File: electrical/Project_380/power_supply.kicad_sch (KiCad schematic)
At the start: 7 parts, among them J5 FL_Motor, J6 FL_Motor, J7 FL_Motor, J8 FL_Motor, U1 HW613

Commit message: added downforce motor control pin
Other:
- title: (none) -> Power Supply
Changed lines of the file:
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@@
 (kicad_sch (version 20211123) (generator eeschema)
   (paper "A4")
+  (title_block
+    (title "Power Supply")
+    (date "2022-02-03")
+    (rev "1.0")
+  )
   (junction (at 48.006 93.726) (diameter 0) (color 0 0 0 0)
   )

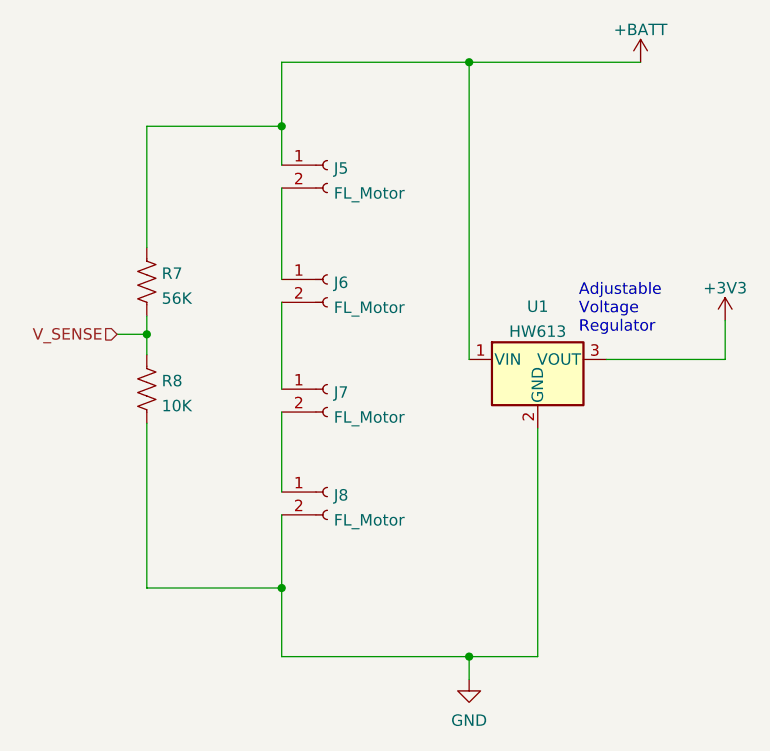
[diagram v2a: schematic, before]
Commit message: added motor controller
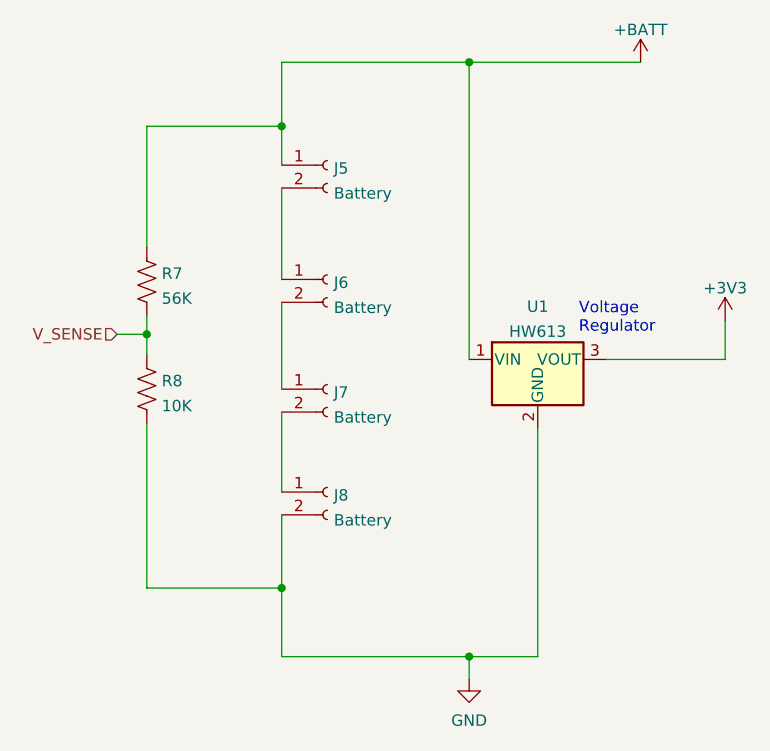
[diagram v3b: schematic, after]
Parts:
- J5, J6, J7, J8: value FL_Motor -> Battery; footprint (none) -> Connector_PinHeader_1.00mm:PinHeader_1x02_P1.00mm_Vertical
- R7, R8: footprint (none) -> Resistor_SMD:R_0603_1608Metric
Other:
- note added: "Voltage Regulator"
- note removed: "Adjustable Voltage Regulator"
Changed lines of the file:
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@@
     (stroke (width 0) (type default) (color 0 0 0 0))
   )
-  (text "Adjustable\nVoltage\nRegulator\n" (at 96.012 93.726 0)
+  (text "Voltage\nRegulator\n" (at 96.012 93.726 0)
     (effects (font (size 1.27 1.27)) (justify left bottom))
   )
@@
   (symbol (lib_id "power:GND") (at 83.82 132.08 0) (unit 1)
     (in_bom yes) (on_board yes) (fields_autoplaced)
-    (property "Reference" "#PWR?" (id 0) (at 83.82 138.43 0)
+    (property "Reference" "#PWR0112" (id 0) (at 83.82 138.43 0)
       (effects (font (size 1.27 1.27)) hide)
     )
@@
       (effects (font (size 1.27 1.27)) (justify right))
     )
-    (property "Footprint" "" (id 2) (at 46.99 87.63 90)
+    (property "Footprint" "Resistor_SMD:R_0603_1608Metric" (id 2) (at 46.99 87.63 90)
       (effects (font (size 1.27 1.27)) hide)
     )
@@
       (effects (font (size 1.27 1.27)) (justify right))
     )
-    (property "Footprint" "" (id 2) (at 46.99 99.568 90)
+    (property "Footprint" "Resistor_SMD:R_0603_1608Metric" (id 2) (at 46.99 99.568 90)
       (effects (font (size 1.27 1.27)) hide)
     )
@@
       (effects (font (size 1.27 1.27)) (justify left))
     )
-    (property "Value" "FL_Motor" (id 1) (at 68.7832 102.9586 0)
+    (property "Value" "Battery" (id 1) (at 68.7832 102.9586 0)
       (effects (font (size 1.27 1.27)) (justify left))
     )
-    (property "Footprint" "" (id 2) (at 68.072 99.822 0)
+    (property "Footprint" "Connector_PinHeader_1.00mm:PinHeader_1x02_P1.00mm_Vertical" (id 2) (at 68.072 99.822 0)
       (effects (font (size 1.27 1.27)) hide)
     )
@@
   (symbol (lib_id "power:+3V3") (at 112.268 92.202 0) (unit 1)
     (in_bom yes) (on_board yes) (fields_autoplaced)
-    (property "Reference" "#PWR?" (id 0) (at 112.268 96.012 0)
+    (property "Reference" "#PWR0114" (id 0) (at 112.268 96.012 0)
       (effects (font (size 1.27 1.27)) hide)
     )
@@
   (symbol (lib_id "power:+BATT") (at 102.87 63.5 0) (unit 1)
     (in_bom yes) (on_board yes) (fields_autoplaced)
-    (property "Reference" "#PWR?" (id 0) (at 102.87 67.31 0)
+    (property "Reference" "#PWR0113" (id 0) (at 102.87 67.31 0)
       (effects (font (size 1.27 1.27)) hide)
     )
@@
       (effects (font (size 1.27 1.27)) (justify left))
     )
-    (property "Value" "FL_Motor" (id 1) (at 68.7832 114.3886 0)
+    (property "Value" "Battery" (id 1) (at 68.7832 114.3886 0)
       (effects (font (size 1.27 1.27)) (justify left))
     )
-    (property "Footprint" "" (id 2) (at 68.072 111.252 0)
+    (property "Footprint" "Connector_PinHeader_1.00mm:PinHeader_1x02_P1.00mm_Vertical" (id 2) (at 68.072 111.252 0)
       (effects (font (size 1.27 1.27)) hide)
     )
@@
       (effects (font (size 1.27 1.27)) (justify left))
     )
-    (property "Value" "FL_Motor" (id 1) (at 68.7832 90.7666 0)
+    (property "Value" "Battery" (id 1) (at 68.7832 90.7666 0)
       (effects (font (size 1.27 1.27)) (justify left))
     )
-    (property "Footprint" "" (id 2) (at 68.072 87.63 0)
+    (property "Footprint" "Connector_PinHeader_1.00mm:PinHeader_1x02_P1.00mm_Vertical" (id 2) (at 68.072 87.63 0)
       (effects (font (size 1.27 1.27)) hide)
     )
@@
       (effects (font (size 1.27 1.27)) (justify left))
     )
-    (property "Value" "FL_Motor" (id 1) (at 68.7832 78.0666 0)
+    (property "Value" "Battery" (id 1) (at 68.7832 78.0666 0)
       (effects (font (size 1.27 1.27)) (justify left))
     )
-    (property "Footprint" "" (id 2) (at 68.072 74.93 0)
+    (property "Footprint" "Connector_PinHeader_1.00mm:PinHeader_1x02_P1.00mm_Vertical" (id 2) (at 68.072 74.93 0)
       (effects (font (size 1.27 1.27)) hide)
     )
